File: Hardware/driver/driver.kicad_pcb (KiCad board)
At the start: 4 copper layers, 128.1 x 184.5 mm, 172 parts, among them J201 Conn_02x10_Odd_Even, J302 Würth 74651194R, J303 Würth 74651194R, J401 TBP02R2W-381-03BE, J402 Conn_01x02_Male, J501 Conn_Coaxial, J601 Screw_Terminal_01x02, K601 EC2-5TNU, M201 Fan_4pin, Q201 MMBT3904, Q202 PN2222A, Q301 IXTH80N075L2, Q302 IXTH80N075L2, Q601 MMBT3904, Q602 MMBT3904, U101 ICL7660, U102 DS2482-100, U103 PI4IOE5V9536, U201 AT24CS32-SSHM, U202 NCP716BCSN330T1G, U203 ADUM1250, U204 FODM217B, U205 FODM217B, U206 EMC2101-R, U301 MCP3421A2T-ECH, U302 OPA2388, U303 DAC60501Z, U304 LM431SC, U305 MCP3421A3T-ECH, U306 OPA2388, U307 DAC60501Z, U308 LM431SC, U309 DS18B20, U310 DS18B20, U501 74LVC1G17, U502 FODM217B, U601 MCP3421A1T-ECH, U602 OPA277

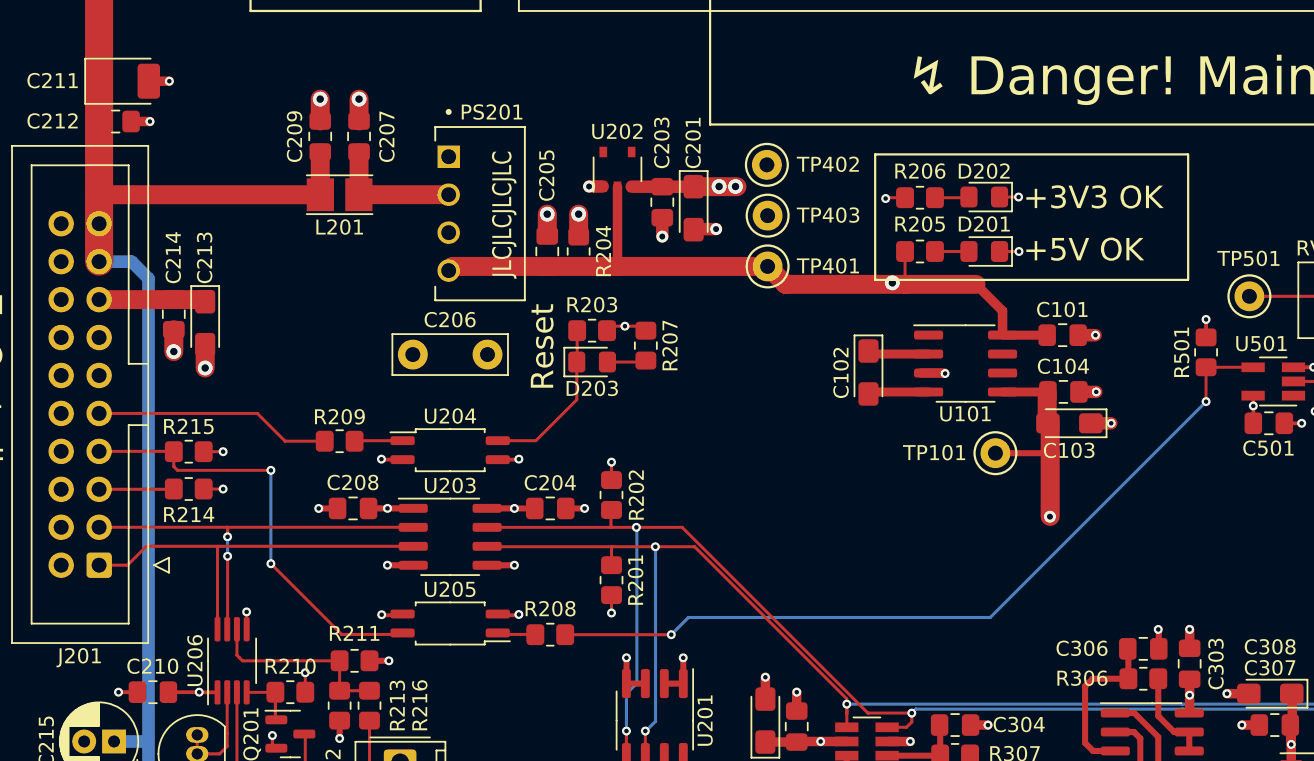
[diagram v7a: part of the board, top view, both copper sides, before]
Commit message: Begin rev2 of driver board
- Improve the power side of things to provide +15V, +12V, +5V, +3V3, and
  -5V on the isolated side of the driver board. This is needed so that
  we can have the +12V for driving opamps with wider swing for the
  drive MOSFETs; these will not turn on with 3V3 as in the original rev1
  design so new driver op amps (U302, U306) need to be chosen
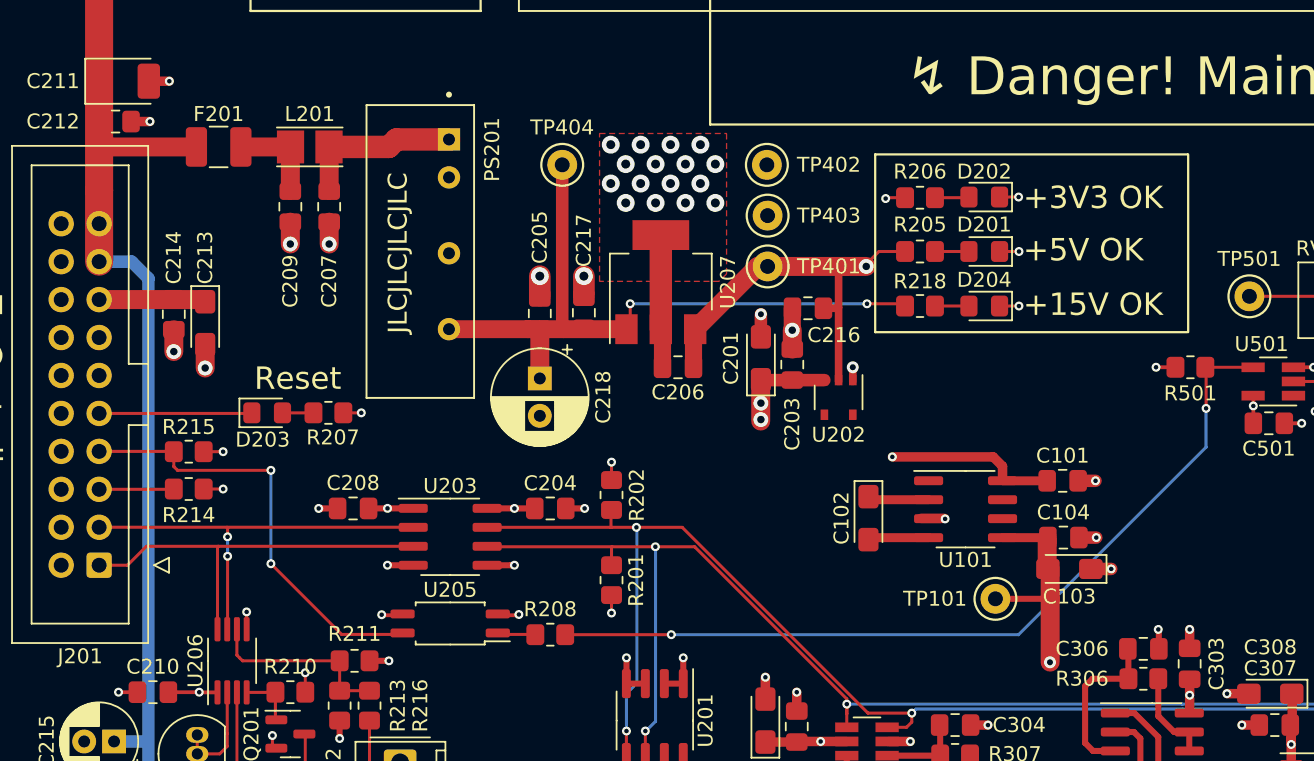
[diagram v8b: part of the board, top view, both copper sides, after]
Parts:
- removed R203: 2k2, Resistor_SMD:R_0805_2012Metric_Pad1.20x1.40mm_HandSolder
- removed R204: 330R, Resistor_SMD:R_0805_2012Metric_Pad1.20x1.40mm_HandSolder
- removed R209: 1k, Resistor_SMD:R_0805_2012Metric_Pad1.20x1.40mm_HandSolder
- removed U204: FODM217B, Package_SO:SOP-4_4.4x2.6mm_P1.27mm
- added C216: 4.7µF, Capacitor_SMD:C_0805_2012Metric_Pad1.18x1.45mm_HandSolder, F.Cu at (76.5, 74.3)
- added C217: 4.7µF, Capacitor_SMD:C_0805_2012Metric_Pad1.18x1.45mm_HandSolder, F.Cu at (61.5, 74.6)
- added C218: 47µF, Capacitor_THT:CP_Radial_D6.3mm_P2.50mm, F.Cu at (58.5, 79.0)
- added D204: Green, LED_SMD:LED_0805_2012Metric_Pad1.15x1.40mm_HandSolder, F.Cu at (88.2, 74.2)
- added F201: 350mA, Fuse:Fuse_1210_3225Metric_Pad1.42x2.65mm_HandSolder, F.Cu at (37.0, 63.5)
- added R218: 7k5, Resistor_SMD:R_0805_2012Metric_Pad1.20x1.40mm_HandSolder, F.Cu at (84.0, 74.2)
- added TP404: +15V, TestPoint:TestPoint_Keystone_5000-5004_Miniature, F.Cu at (60.0, 64.7)
- added U207: MCP1703AT-5002E/DB, Package_TO_SOT_SMD:SOT-223-3_TabPin2, F.Cu at (66.6, 72.5)
- C206: value 330pF Y -> 4.7µF; footprint Capacitor_THT:C_Disc_D7.5mm_W2.5mm_P5.00mm -> Capacitor_SMD:C_0805_2012Metric_Pad1.18x1.45mm_HandSolder
- PS201: value PDSE1-S12-S5-S -> PCN2-S12-S15-S; footprint programmable-load:CONV_PDSE1-S12-S3-S -> programmable-load:CONV_PCN2-S12-S15-S
- moved D203 22.0 mm to (40.2, 81.3)
- moved R207 21.7 mm to (44.4, 81.3), turned to 180 degrees
- moved U202 21.3 mm to (78.5, 80.3), turned to -90 degrees
- moved C203 13.9 mm to (75.4, 78.1), turned to 90 degrees
- moved C206 12.8 mm to (67.8, 78.2)
- moved C201 11.0 mm to (73.3, 77.7), turned to 90 degrees
- moved C101 9.75 mm to (93.5, 85.8)
- moved C102 9.75 mm to (80.5, 88.3)
- moved C103 9.75 mm to (94.0, 91.8)
- moved C104 9.75 mm to (93.5, 89.7)
- moved TP101 9.75 mm to (89.0, 93.8)
- moved U101 9.75 mm to (87.0, 87.8)
- moved PS201 5.39 mm to (52.4, 63.0)
- moved C207 5.11 mm to (44.4, 67.5), turned to -90 degrees
- moved C209 5.11 mm to (41.8, 67.5), turned to -90 degrees
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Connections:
- C205 pad 1: +5V -> +15V
- C206 pad 1: GND -> +5V
- C206 pad 2: GNDA -> GND
- C209 pad 1: +12VA -> Net-(C209-Pad1)
- D203 pad 1: /~{RESET} -> /External Interface/~{EXT_RESET}
- L201 pad 2: +12VA -> Net-(C209-Pad1)
- PS201 pad 1: GNDA -> Net-(C207-Pad1)
- PS201 pad 2: Net-(C207-Pad1) -> GNDA
- PS201 pad 4: +5V -> GND
- R207 pad 1: +3V3 -> +3V3A
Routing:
- net +15V: track 0.00 -> 46.4 mm, vias 0 -> 2
- net +12VA: track 145.1 -> 133.5 mm
- net /~{RESET}: track 11.1 -> 0.00 mm
- net -5V: track 174.9 -> 165.1 mm
- net +5V: track 234.9 -> 225.7 mm, vias 2 -> 3
- net GND: track 98.4 -> 107.6 mm, vias 70 -> 86
- net Net-(C209-Pad1): track 0.00 -> 6.11 mm
- net /External Interface/~{EXT_RESET}: track 15.9 -> 10.6 mm
- net Net-(R209-Pad2): track 3.23 -> 0.00 mm
- net +3V3: track 66.1 -> 63.4 mm, vias 22 -> 21
- net GNDA: track 42.3 -> 40.0 mm, vias 23 -> 22
- net Net-(D204-Pad2): track 0.00 -> 2.27 mm
- net Net-(C207-Pad1): track 8.82 -> 11.0 mm
- net /TRIGGER: track 55.3 -> 57.1 mm
- net +3V3A: track 19.8 -> 21.0 mm, vias 7 -> 8
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- added copper zone on F.Cu, net GND
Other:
- board text added: "+15V OK"
